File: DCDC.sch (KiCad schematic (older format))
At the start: 26 parts, among them U7 TPS54561DPRR, U9 PDS760-13

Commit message: Finished first version of schematic
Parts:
- removed C28, C29, C30: 2.2u, Capacitor_SMD:C_1206_3216Metric, symbol Device:C_Small
- removed C36, C37: 2.2u, Capacitor_SMD:C_0603_1608Metric, symbol Device:C_Small
- removed C38: 100u, Capacitor_THT:CP_Radial_D10.0mm_P5.00mm, symbol Device:CP_Small
- added C11, C12: 100u, Capacitor_THT:CP_Radial_D10.0mm_P5.00mm, symbol Device:CP_Small
- added Q1, Q2, Q3, Q4, Q5: Q_NMOS_GSD, Package_TO_SOT_SMD:SOT-23, symbol Device:Q_NMOS_GSD
- added R18: 2.2k, Resistor_SMD:R_0603_1608Metric, symbol Device:R_Small
- added R22: 2k, Resistor_SMD:R_0603_1608Metric, symbol Device:R_Small
- added R23: 4k, Resistor_SMD:R_0603_1608Metric, symbol Device:R_Small
- added R24: 8k, Resistor_SMD:R_0603_1608Metric, symbol Device:R_Small
- added R25: 16k, Resistor_SMD:R_0603_1608Metric, symbol Device:R_Small
- C13: renamed from C39; value 470u -> 100u
- R19: value 53.6k -> 56k
- R20: value 10.2k -> 1k
- U5: renamed from U9; OrderN (none) -> PDS760DICT-ND
- renumbered C31 to C10, C27 to C14, C33 to C15, C32 to C16, C34 to C17, C40 to C18, C16 to C19, C35 to C9, L3 to L1, R15 to R21, R16 to R26, R17 to R27, R18 to R28, R11 to R29, R12 to R30, U7 to U6
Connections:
- net FB: now also R22.2, R23.2, R24.2, R25.2
- net GND: now also C11.2, C12.2, Q1.2 (S), Q2.2 (S), Q3.2 (S), Q4.2 (S), Q5.2 (S), R18.2; no longer R20.1
- net OUT_RAIL: now also C11.1, C12.1
- net ENABLE: now reaches U6.3 (EN)
- net ENABLE: now also R18.1
- new net: Q2.3 (D), R22.1
- new net: Q4.3 (D), R24.1
- new net: Q3.3 (D), R23.1
- new net: Q5.3 (D), R25.1
- new net: Q1.3 (D), R20.1
- new net VSEL1: Q1.1 (G)
- new net VSEL2: Q2.1 (G)
- new net VSEL3: Q3.1 (G)
- new net VSEL4: Q4.1 (G)
- new net VSEL5: Q5.1 (G)
- no-connect marks 2 -> 1
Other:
- note removed: "12061C225KAT2A CAP CER 2.2UF 100V X7R 1206\nC3216X7S2A225K160AB CAP CER 2.2UF 100V X7S 1206\n"
- moved on the sheet: C10, C13, C14, C15, C16, C17, C18, C19, C9, L1, R19, R21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

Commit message: Finished routing and added some 3D models
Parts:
- L1: OrderN (none) -> 732-1241-1-ND
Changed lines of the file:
@@
 F 2 "Inductor_SMD:L_12x12mm_H8mm" H 1800 4800 50  0001 C CNN
 F 3 "~" H 1800 4800 50  0001 C CNN
+F 4 "732-1241-1-ND" V 1800 4800 50  0001 C CNN "OrderN"
 	1    1800 4800
 	0    -1   -1   0

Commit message: almost done with bom. there are some issues
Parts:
- C10: OrderN (none) -> 445-5207-1-ND
- C11, C12, C13: OrderN (none) -> 493-11829-1-ND
- C14: OrderN (none) -> 1276-1009-1-ND
- C15, C18, C19: OrderN (none) -> 1276-1000-1-ND
- C16: OrderN (none) -> 1276-1098-1-ND
- C17: OrderN (none) -> 399-1056-1-ND
- C9: OrderN (none) -> 490-10731-1-ND
- R18, R28, R30: OrderN (none) -> 311-2.20KHRCT-ND
- R19: OrderN (none) -> 311-56KHRCT-ND
- R20: OrderN (none) -> 311-1.00KHRCT-ND
- R21: OrderN (none) -> 311-243KHRCT-ND
- R22: OrderN (none) -> 311-2.00KHRCT-ND
- R25: OrderN (none) -> 311-16.0KHRCT-ND
- R26: OrderN (none) -> 311-16.9KHRCT-ND
- R27, R29: OrderN (none) -> 311-39.0KHRCT-ND
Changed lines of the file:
@@
 F 2 "Resistor_SMD:R_0603_1608Metric" H 8150 1700 50  0001 C CNN
 F 3 "~" H 8150 1700 50  0001 C CNN
+F 4 "311-39.0KHRCT-ND" H 8150 1700 50  0001 C CNN "OrderN"
 	1    8150 1700
 	1    0    0    -1
@@
 F 2 "Resistor_SMD:R_0603_1608Metric" H 8150 2150 50  0001 C CNN
 F 3 "~" H 8150 2150 50  0001 C CNN
+F 4 " 311-2.20KHRCT-ND" H 8150 2150 50  0001 C CNN "OrderN"
 	1    8150 2150
 	1    0    0    -1
@@
 F 3 "~" H 3050 5150 50  0001 C CNN
 F 4 "https://www.digikey.se/product-detail/en/nichicon/URS1C471MPD1TD/493-11709-1-ND/4320195" H 3050 5150 50  0001 C CNN "digikey"
+F 5 "493-11829-1-ND" H 3050 5150 50  0001 C CNN "OrderN"
 	1    3050 5150
 	1    0    0    -1
@@
 F 2 "Capacitor_SMD:C_0603_1608Metric" H 8350 2150 50  0001 C CNN
 F 3 "~" H 8350 2150 50  0001 C CNN
+F 4 "1276-1000-1-ND" H 8350 2150 50  0001 C CNN "OrderN"
 	1    8350 2150
 	1    0    0    -1
@@
 F 2 "Capacitor_SMD:C_1206_3216Metric" H 2250 2700 50  0001 C CNN
 F 3 "~" H 2250 2700 50  0001 C CNN
+F 4 "445-5207-1-ND" H 2250 2700 50  0001 C CNN "OrderN"
 	1    2250 2700
 	1    0    0    -1
@@
 F 2 "Resistor_SMD:R_0603_1608Metric" H 4100 3350 50  0001 C CNN
 F 3 "~" H 4100 3350 50  0001 C CNN
+F 4 "311-243KHRCT-ND" H 4100 3350 50  0001 C CNN "OrderN"
 	1    4100 3350
 	1    0    0    -1
@@
 F 2 "Capacitor_SMD:C_0603_1608Metric" H 3850 3350 50  0001 C CNN
 F 3 "~" H 3850 3350 50  0001 C CNN
+F 4 "1276-1009-1-ND" H 3850 3350 50  0001 C CNN "OrderN"
 	1    3850 3350
 	1    0    0    -1
@@
 F 2 "Capacitor_SMD:C_0603_1608Metric" H 6750 3350 50  0001 C CNN
 F 3 "~" H 6750 3350 50  0001 C CNN
+F 4 "399-1056-1-ND" H 6750 3350 50  0001 C CNN "OrderN"
 	1    6750 3350
 	1    0    0    -1
@@
 F 2 "Resistor_SMD:R_0603_1608Metric" H 6350 3100 50  0001 C CNN
 F 3 "~" H 6350 3100 50  0001 C CNN
+F 4 " 311-16.9KHRCT-ND " H 6350 3100 50  0001 C CNN "OrderN"
 	1    6350 3100
 	1    0    0    -1
@@
 F 2 "Capacitor_SMD:C_0603_1608Metric" H 6350 3350 50  0001 C CNN
 F 3 "~" H 6350 3350 50  0001 C CNN
+F 4 "1276-1098-1-ND" H 6350 3350 50  0001 C CNN "OrderN"
 	1    6350 3350
 	1    0    0    -1
@@
 F 2 "Capacitor_SMD:C_0603_1608Metric" H 6200 2100 50  0001 C CNN
 F 3 "~" H 6200 2100 50  0001 C CNN
+F 4 "1276-1000-1-ND" H 6200 2100 50  0001 C CNN "OrderN"
 	1    6200 2100
 	1    0    0    -1
@@
 F 2 "Resistor_SMD:R_0603_1608Metric" H 3600 5000 50  0001 C CNN
 F 3 "~" H 3600 5000 50  0001 C CNN
+F 4 " 311-56KHRCT-ND " H 3600 5000 50  0001 C CNN "OrderN"
 	1    3600 5000
 	-1   0    0    1
@@
 F 2 "Capacitor_SMD:C_0603_1608Metric" H 8350 3550 50  0001 C CNN
 F 3 "~" H 8350 3550 50  0001 C CNN
+F 4 "1276-1000-1-ND" H 8350 3550 50  0001 C CNN "OrderN"
 	1    8350 3550
 	1    0    0    -1
@@
 F 2 "Resistor_SMD:R_0603_1608Metric" H 8150 3100 50  0001 C CNN
 F 3 "~" H 8150 3100 50  0001 C CNN
+F 4 "311-39.0KHRCT-ND" H 8150 3100 50  0001 C CNN "OrderN"
 	1    8150 3100
 	1    0    0    -1
@@
 F 2 "Resistor_SMD:R_0603_1608Metric" H 8150 3550 50  0001 C CNN
 F 3 "~" H 8150 3550 50  0001 C CNN
+F 4 " 311-2.20KHRCT-ND" H 8150 3550 50  0001 C CNN "OrderN"
 	1    8150 3550
 	1    0    0    -1
@@
 F 2 "Resistor_SMD:R_0603_1608Metric" H 3250 2900 50  0001 C CNN
 F 3 "~" H 3250 2900 50  0001 C CNN
+F 4 " 311-2.20KHRCT-ND" H 3250 2900 50  0001 C CNN "OrderN"
 	1    3250 2900
 	1    0    0    -1
@@
 F 2 "Resistor_SMD:R_0603_1608Metric" H 3600 5400 50  0001 C CNN
 F 3 "~" H 3600 5400 50  0001 C CNN
+F 4 " 311-1.00KHRCT-ND " H 3600 5400 50  0001 C CNN "OrderN"
 	1    3600 5400
 	-1   0    0    1
@@
 F 2 "Resistor_SMD:R_0603_1608Metric" H 4200 5400 50  0001 C CNN
 F 3 "~" H 4200 5400 50  0001 C CNN
+F 4 "311-2.00KHRCT-ND" H 4200 5400 50  0001 C CNN "OrderN"
 	1    4200 5400
 	-1   0    0    1
@@
 F 2 "Resistor_SMD:R_0603_1608Metric" H 6050 5400 50  0001 C CNN
 F 3 "~" H 6050 5400 50  0001 C CNN
+F 4 "311-16.0KHRCT-ND " H 6050 5400 50  0001 C CNN "OrderN"
 	1    6050 5400
 	-1   0    0    1
@@
 F 3 "~" H 2750 5150 50  0001 C CNN
 F 4 "https://www.digikey.se/product-detail/en/nichicon/URS1C471MPD1TD/493-11709-1-ND/4320195" H 2750 5150 50  0001 C CNN "digikey"
+F 5 "493-11829-1-ND" H 2750 5150 50  0001 C CNN "OrderN"
 	1    2750 5150
 	1    0    0    -1
@@
 F 3 "~" H 2400 5150 50  0001 C CNN
 F 4 "https://www.digikey.se/product-detail/en/nichicon/URS1C471MPD1TD/493-11709-1-ND/4320195" H 2400 5150 50  0001 C CNN "digikey"
+F 5 "493-11829-1-ND" H 2400 5150 50  0001 C CNN "OrderN"
 	1    2400 5150
 	1    0    0    -1
@@
 F 2 "Capacitor_SMD:C_0603_1608Metric" H 2050 5150 50  0001 C CNN
 F 3 "~" H 2050 5150 50  0001 C CNN
+F 4 "490-10731-1-ND" H 2050 5150 50  0001 C CNN "OrderN"
 	1    2050 5150
 	1    0    0    -1

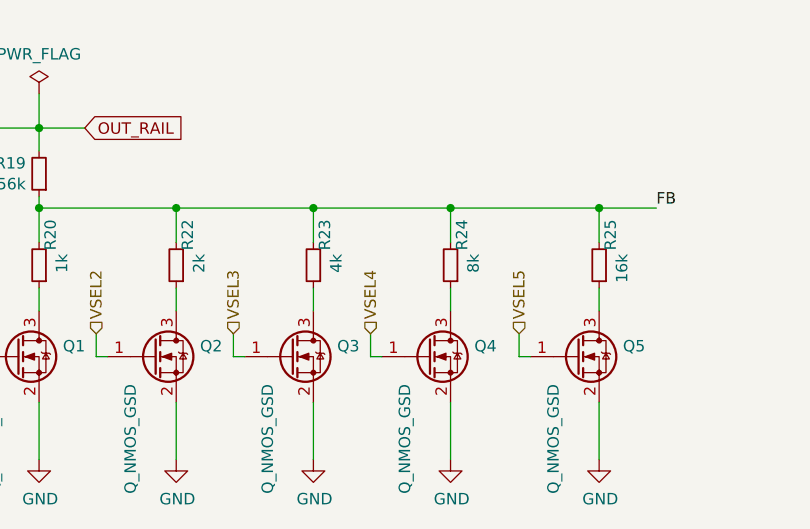
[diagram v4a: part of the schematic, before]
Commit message: added new resistances for the resistance ladder-thingy
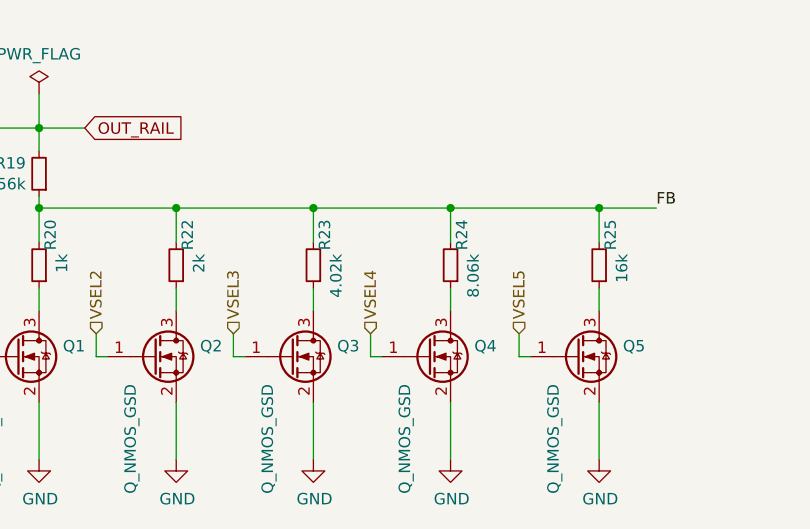
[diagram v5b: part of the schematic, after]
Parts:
- R22: OrderN 311-2.00KHRCT-ND -> 311-2.00KHRCT-ND
- R23: value 4k -> 4.02k; OrderN (none) -> 311-4.02KHRTR-ND
- R24: value 8k -> 8.06k; OrderN (none) -> 311-8.06KHRCT-ND
- R25: OrderN 311-16.0KHRCT-ND -> 311-16.0KHRCT-ND
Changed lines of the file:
@@
 F 2 "Resistor_SMD:R_0603_1608Metric" H 4200 5400 50  0001 C CNN
 F 3 "~" H 4200 5400 50  0001 C CNN
-F 4 "311-2.00KHRCT-ND" H 4200 5400 50  0001 C CNN "OrderN"
+F 4 " 311-2.00KHRCT-ND " H 4200 5400 50  0001 C CNN "OrderN"
 	1    4200 5400
 	-1   0    0    1
@@
 P 4800 5400
 F 0 "R23" V 4750 5200 50  0000 L CNN
-F 1 "4k" V 4700 5350 50  0000 L CNN
+F 1 "4.02k" V 4700 5350 50  0000 L CNN
 F 2 "Resistor_SMD:R_0603_1608Metric" H 4800 5400 50  0001 C CNN
 F 3 "~" H 4800 5400 50  0001 C CNN
+F 4 " 311-4.02KHRTR-ND" H 4800 5400 50  0001 C CNN "OrderN"
 	1    4800 5400
 	-1   0    0    1
@@
 P 5400 5400
 F 0 "R24" V 5350 5200 50  0000 L CNN
-F 1 "8k" V 5300 5350 50  0000 L CNN
+F 1 "8.06k" V 5300 5350 50  0000 L CNN
 F 2 "Resistor_SMD:R_0603_1608Metric" H 5400 5400 50  0001 C CNN
 F 3 "~" H 5400 5400 50  0001 C CNN
+F 4 " 311-8.06KHRCT-ND " H 5400 5400 50  0001 C CNN "OrderN"
 	1    5400 5400
 	-1   0    0    1
@@
 F 2 "Resistor_SMD:R_0603_1608Metric" H 6050 5400 50  0001 C CNN
 F 3 "~" H 6050 5400 50  0001 C CNN
-F 4 "311-16.0KHRCT-ND " H 6050 5400 50  0001 C CNN "OrderN"
+F 4 " 311-16.0KHRCT-ND " H 6050 5400 50  0001 C CNN "OrderN"
 	1    6050 5400
 	-1   0    0    1

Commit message: tweak component matrix
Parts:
- R23: OrderN 311-4.02KHRTR-ND -> 311-4.02KHRCT-ND
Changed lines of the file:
@@
 F 2 "Resistor_SMD:R_0603_1608Metric" H 4800 5400 50  0001 C CNN
 F 3 "~" H 4800 5400 50  0001 C CNN
-F 4 " 311-4.02KHRTR-ND" H 4800 5400 50  0001 C CNN "OrderN"
+F 4 "311-4.02KHRCT-ND " H 4800 5400 50  0001 C CNN "OrderN"
 	1    4800 5400
 	-1   0    0    1
